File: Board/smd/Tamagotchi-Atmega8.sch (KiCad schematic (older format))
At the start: 27 parts, among them J1 Conn_02x05_Odd_Even, J2 Conn_01x02, J3 Conn_01x04, J4 Conn_01x07, J5 Conn_01x02, Q1 Q_NPN_BEC, SW1 SW_Push, U1 AMS1117, U2 ATmega328-AU, U3 DS1307Z+, X1 8MHz, X2 32768kHz

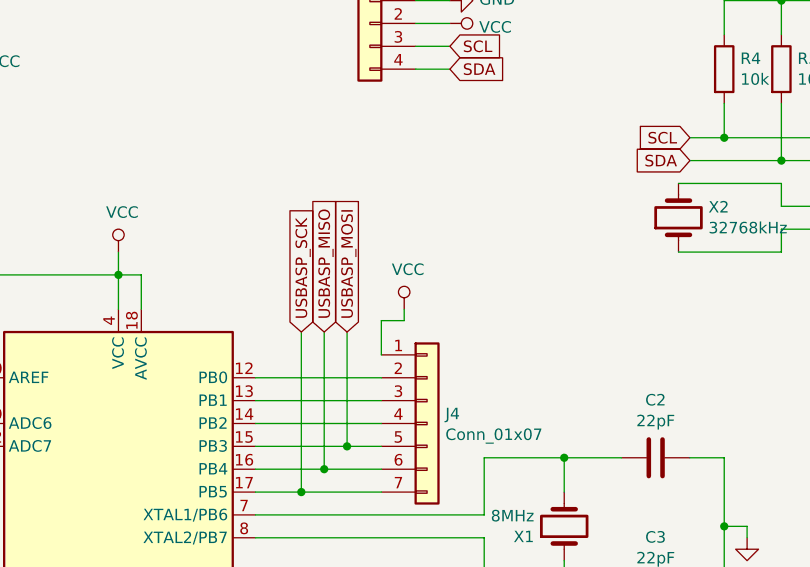
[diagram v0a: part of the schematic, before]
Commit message: fixed buttons polarity (pull-up state and negative activation)
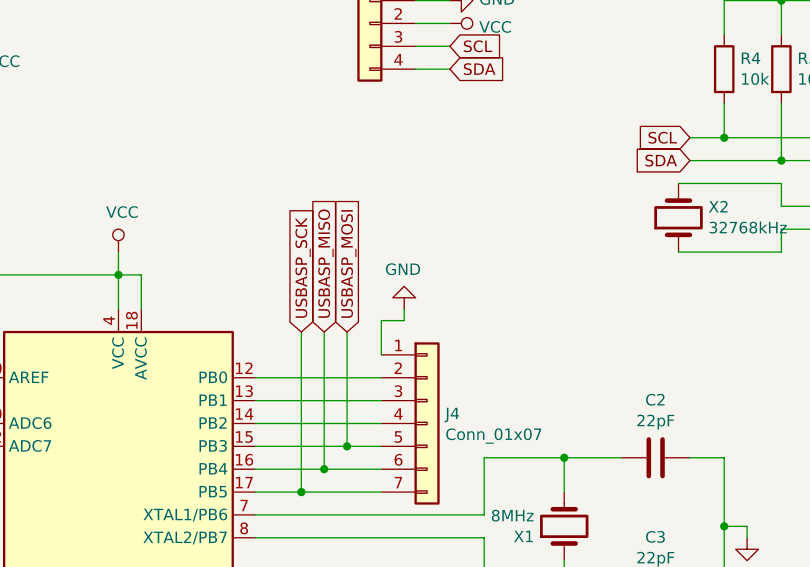
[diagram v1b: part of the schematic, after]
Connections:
- net GND: now also J4.1 (Pin_1)
- net VCC: no longer J4.1 (Pin_1)
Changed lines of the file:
@@
 	5250 2550 5250 2500
 $Comp
-L power:VCC #PWR0101
-U 1 1 5E397814
+L power:GND #PWR?
+U 1 1 5E3A60C5
 P 5250 2500
-F 0 "#PWR0101" H 5250 2350 50  0001 C CNN
-F 1 "VCC" H 5267 2673 50  0000 C CNN
+F 0 "#PWR?" H 5250 2250 50  0001 C CNN
+F 1 "GND" H 5255 2327 50  0000 C CNN
 F 2 "" H 5250 2500 50  0001 C CNN
 F 3 "" H 5250 2500 50  0001 C CNN
 	1    5250 2500
-	1    0    0    -1
+	-1   0    0    1
 $EndComp
 $EndSCHEMATC
